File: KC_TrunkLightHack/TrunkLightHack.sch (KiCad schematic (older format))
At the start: 22 parts, among them P1 CONN_01X01, P2 CONN_01X01, Q1 ZVN3306A, Q2 2N3904TFCT, Q3 STS7P4LLF6, Q4 ZVN3306A, SW1 Trunk_Switch

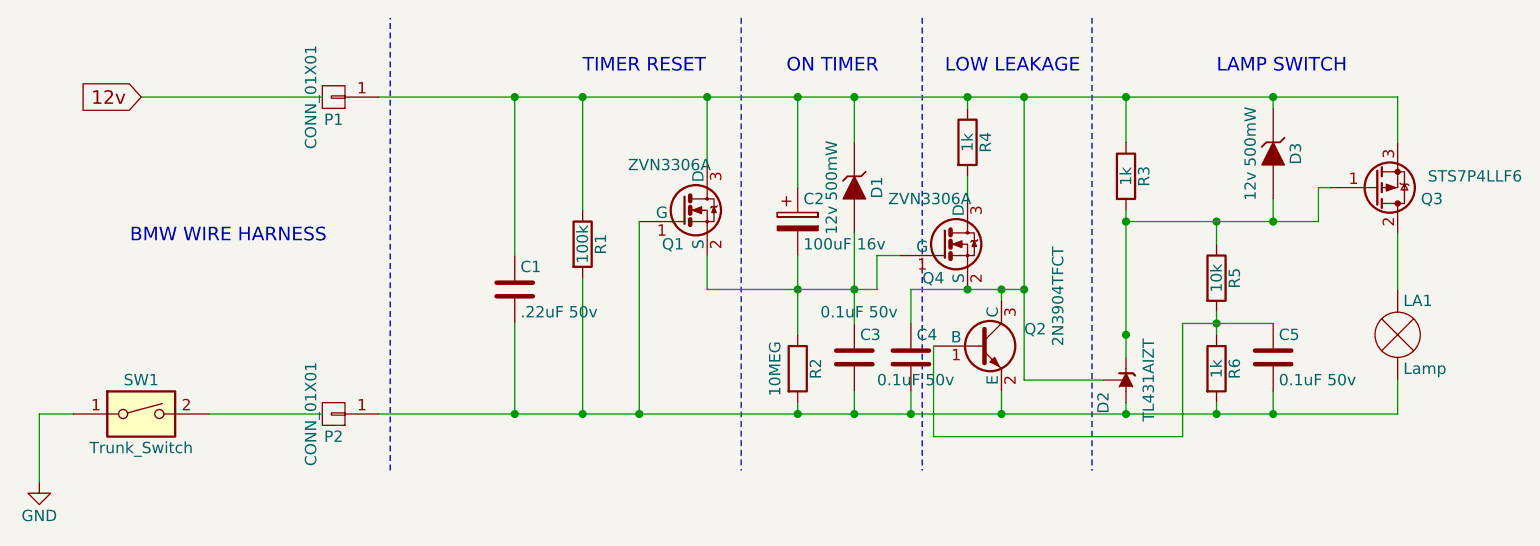
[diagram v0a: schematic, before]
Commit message: Latest Schematic Changes
A 15 Analog Timer for the BMW
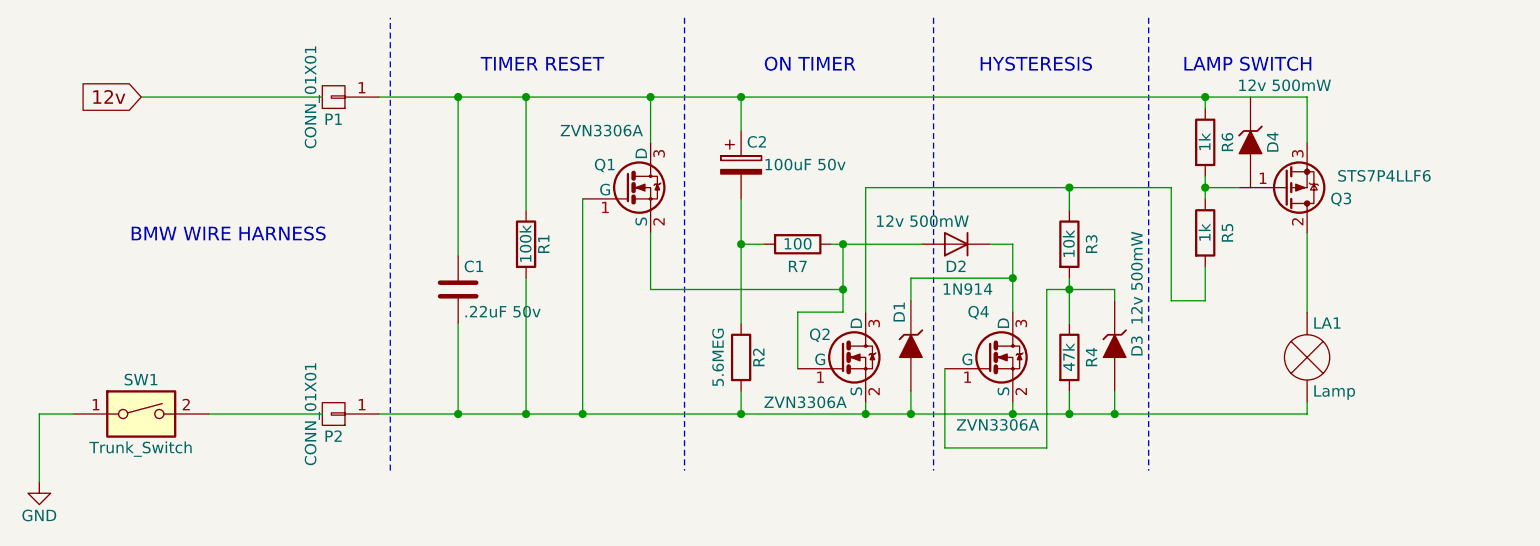
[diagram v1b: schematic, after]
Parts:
- removed C3, C4, C5: 0.1uF 50v, symbol C
- removed D2: TL431AIZT, TO-92, symbol TL431LP
- removed Q2: 2N3904TFCT, SOT-23, symbol MMBT3904
- added D2: 1N914, Diodes_THT:D_DO-35_SOD27_Horizontal_RM10, symbol 1N914
- added D4: 12v 500mW, symbol ZENER
- added Q2: ZVN3306A, TO_92, symbol 2N7002
- added R7: 100, symbol R
- C2: value 100uF 16v -> 100uF 50v
- Q1, Q4: footprint TO_SOT_Packages_SMD:SOT-23 -> TO_92
- R2: value 10MEG -> 5.6MEG
- R3: value 1k -> 10k
- R4: value 1k -> 47k
- R5: value 10k -> 1k
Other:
- note added: "HYSTERESIS\n"
- note removed: "LOW LEAKAGE\n"
- moved on the sheet: C1, C2, D3, LA1, Q3, R1, R2, R6
